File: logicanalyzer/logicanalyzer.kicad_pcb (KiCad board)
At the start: 2 copper layers, 82.5 x 83.8 mm, 76 parts, among them J1 Conn_02x17_Odd_Even, J2 Conn_01x30_Pin, U1 74HC04, U10 74151, U2 74HC595, U3 74HC595, U4 74HC86, U5 74151, U6 74LS32, U7 74HC86, U8 74151

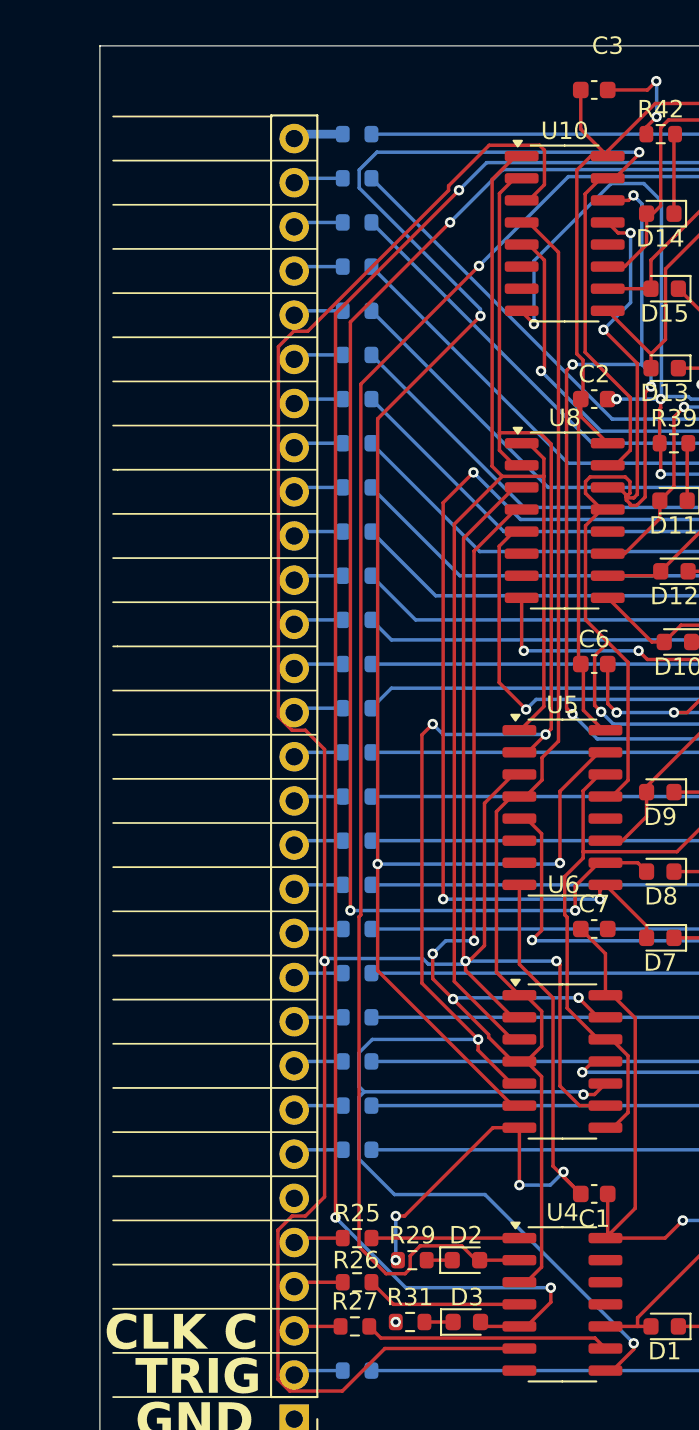
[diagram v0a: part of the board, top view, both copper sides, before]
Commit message: Schematic changes
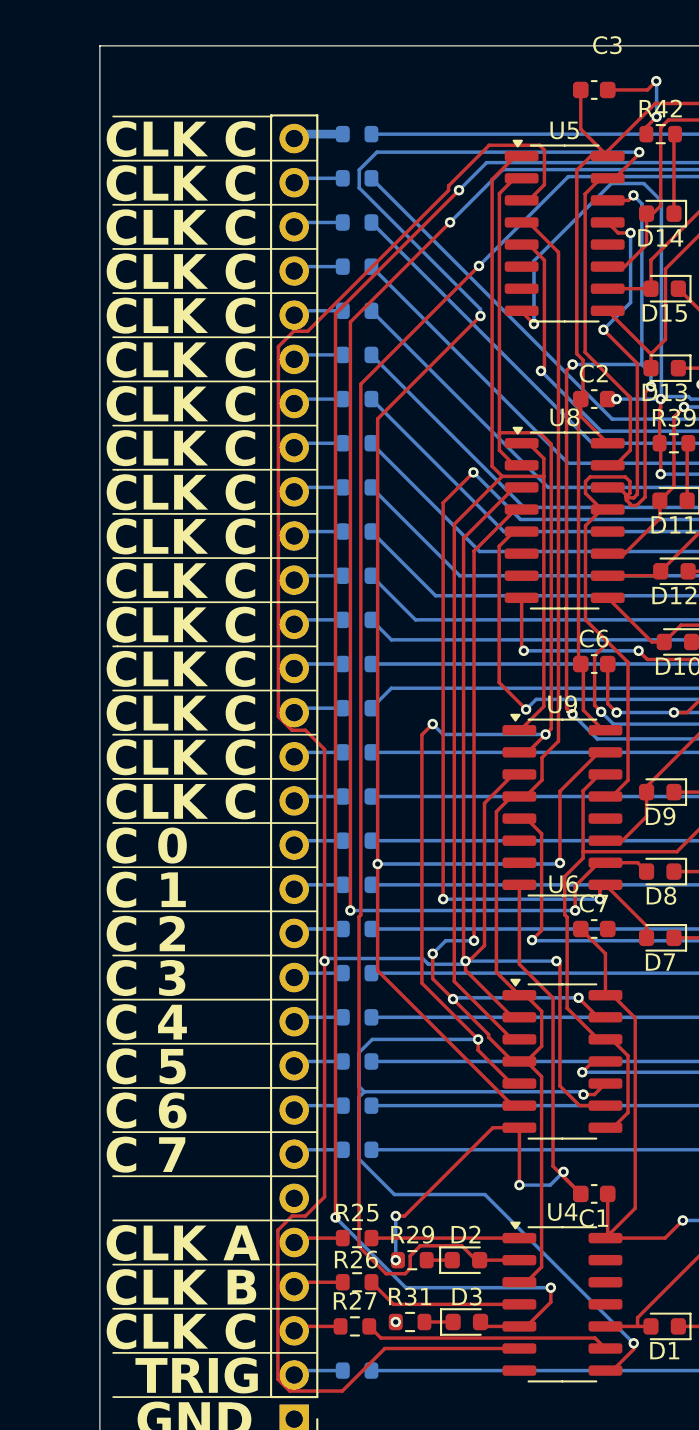
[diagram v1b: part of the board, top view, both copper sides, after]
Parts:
- removed U10: 74151, Package_SO:SOIC-16_3.9x9.9mm_P1.27mm
- added U9: 74HC251, Package_SO:SOIC-16_3.9x9.9mm_P1.27mm, F.Cu at (71.1, 92.1)
- R1, R10, R11, R12, R13, R14, R15, R16, R17, R18, R19, R2, R20, R21, R22, R23, R24, R25, R26, R27, R28, R29, R3, R30, R31, R32, R33, R34, R35, R36, R37, R38, R39, R4, R40, R41, R42, R43, R5, R6, R7, R8, R9: value 33k -> 500
- U5, U8: value 74151 -> 74HC251
- U6: value 74LS32 -> 74HC32
- moved U5 33.0 mm to (71.2, 59.1)
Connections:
- J1 pad 11: A7 -> A0
- J1 pad 12: A6 -> A1
- J1 pad 13: A5 -> A2
- J1 pad 14: A4 -> A3
- J1 pad 15: A3 -> A4
- J1 pad 16: A2 -> A5
- J1 pad 17: A1 -> A6
- J1 pad 18: A0 -> A7
- J1 pad 19: B7 -> B0
- J1 pad 20: B6 -> B1
- J1 pad 21: B5 -> B2
- J1 pad 22: B4 -> B3
- J1 pad 23: B3 -> B4
- J1 pad 24: B2 -> B5
- J1 pad 25: B1 -> B6
- J1 pad 26: B0 -> B7
- J1 pad 27: C7 -> C0
- J1 pad 28: C6 -> C1
- J1 pad 29: C5 -> C2
- J1 pad 30: C4 -> C3
- J1 pad 31: C3 -> C4
- J1 pad 32: C2 -> C5
- J1 pad 33: C1 -> C6
- J1 pad 34: C0 -> C7
- J2 pad 1: unconnected-(J2-Pin_1-Pad1) -> GND
- R1 pad 2: A6 -> A1
- R10 pad 2: B5 -> B2
- R11 pad 2: B4 -> B3
- R12 pad 2: B3 -> B4
- R13 pad 2: B2 -> B5
- R14 pad 2: B1 -> B6
- R15 pad 2: B0 -> B7
- R16 pad 2: C7 -> C0
- R17 pad 2: C6 -> C1
- R18 pad 2: C5 -> C2
- R19 pad 2: C4 -> C3
- R2 pad 2: A5 -> A2
- R20 pad 2: C3 -> C4
- R21 pad 2: C2 -> C5
- R22 pad 2: C1 -> C6
- R23 pad 2: C0 -> C7
- R3 pad 2: A4 -> A3
- R30 pad 2: A7 -> A0
- R4 pad 2: A3 -> A4
- R5 pad 2: A2 -> A5
- R6 pad 2: A1 -> A6
- R7 pad 2: A0 -> A7
- R8 pad 2: B7 -> B0
- R9 pad 2: B6 -> B1
- U5 pad 10: SMPL_A_is_C -> SMPL_C_is_C
- U5 pad 11: SMPL_A_is_B -> SMPL_C_is_B
- U5 pad 9: SMPL_A_is_A+C -> SMPL_C_is_A+C
- U7 pad 1: Net-(U5-Q) -> Net-(U9-Q)
- U7 pad 9: Net-(U10-Q) -> Net-(U5-Q)
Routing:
- net Net-(U9-Q): track 0.00 -> 65.7 mm, vias 0 -> 4
- net Net-(U10-Q): track 41.7 -> 0.00 mm, vias 2 -> 0
- net Net-(U5-Q): track 65.7 -> 41.7 mm, vias 4 -> 2
- net C7: track 53.8 -> 60.5 mm
- net C0: track 60.5 -> 53.8 mm
- net A6: track 60.4 -> 54.8 mm
- net A1: track 54.8 -> 60.4 mm
- net C5: track 54.8 -> 59.5 mm
- net C2: track 59.5 -> 54.8 mm
- net B4: track 55.2 -> 51.7 mm
- net B3: track 51.7 -> 55.2 mm
- net B6: track 56.2 -> 52.7 mm
- net B1: track 52.7 -> 56.2 mm
- net A4: track 59.4 -> 55.9 mm
- net A3: track 55.9 -> 59.4 mm
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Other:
- board text added: "C 0"
- board text added: "C 1"
- board text added: "C 2"
- board text added: "C 3"
- board text added: "C 4"
- board text added: "C 5"
- board text added: "C 6"
- board text added: "C 7"
- board text added: "CLK A"
- board text added: "CLK B"

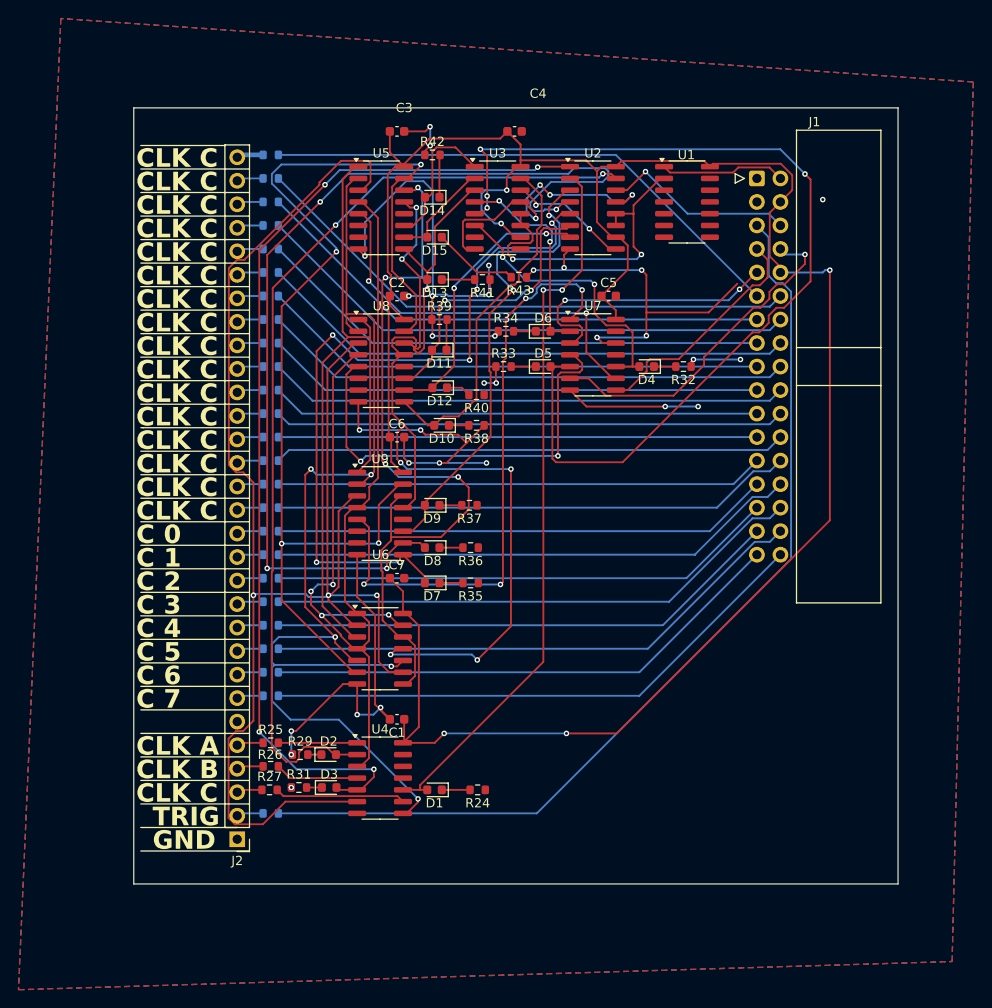
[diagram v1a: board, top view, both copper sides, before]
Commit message: Schematic changes
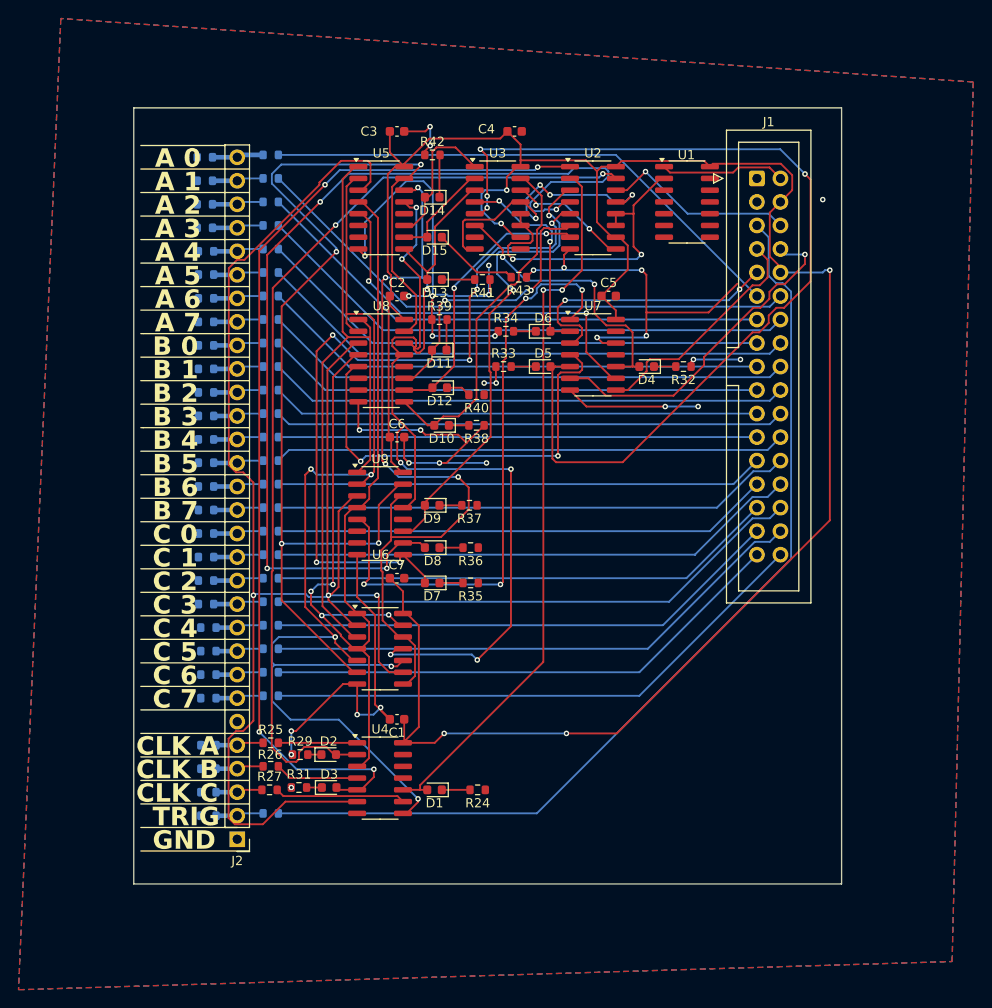
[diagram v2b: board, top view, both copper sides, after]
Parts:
- added R44: 100k, Resistor_SMD:R_0603_1608Metric, B.Cu at (52.5, 124.7)
- added R45: 100k, Resistor_SMD:R_0603_1608Metric, B.Cu at (52.5, 122.2)
- added R46: 100k, Resistor_SMD:R_0603_1608Metric, B.Cu at (52.5, 119.6)
- added R47: 100k, Resistor_SMD:R_0603_1608Metric, B.Cu at (52.5, 117.1)
- added R48: 100k, Resistor_SMD:R_0603_1608Metric, B.Cu at (52.5, 112.0)
- added R49: 100k, Resistor_SMD:R_0603_1608Metric, B.Cu at (52.5, 109.5)
- added R50: 100k, Resistor_SMD:R_0603_1608Metric, B.Cu at (52.5, 106.9)
- added R51: 100k, Resistor_SMD:R_0603_1608Metric, B.Cu at (52.5, 104.4)
- added R52: 100k, Resistor_SMD:R_0603_1608Metric, B.Cu at (52.3, 101.9)
- added R53: 100k, Resistor_SMD:R_0603_1608Metric, B.Cu at (52.3, 99.3)
- added R54: 100k, Resistor_SMD:R_0603_1608Metric, B.Cu at (52.3, 96.8)
- added R55: 100k, Resistor_SMD:R_0603_1608Metric, B.Cu at (52.3, 94.2)
- added R56: 100k, Resistor_SMD:R_0603_1608Metric, B.Cu at (52.3, 91.7)
- added R57: 100k, Resistor_SMD:R_0603_1608Metric, B.Cu at (52.3, 89.2)
- added R58: 100k, Resistor_SMD:R_0603_1608Metric, B.Cu at (52.3, 86.6)
- added R59: 100k, Resistor_SMD:R_0603_1608Metric, B.Cu at (52.3, 84.1)
- added R60: 100k, Resistor_SMD:R_0603_1608Metric, B.Cu at (52.3, 81.5)
- added R61: 100k, Resistor_SMD:R_0603_1608Metric, B.Cu at (52.3, 79.0)
- added R62: 100k, Resistor_SMD:R_0603_1608Metric, B.Cu at (52.3, 76.5)
- added R63: 100k, Resistor_SMD:R_0603_1608Metric, B.Cu at (52.3, 73.9)
- added R64: 100k, Resistor_SMD:R_0603_1608Metric, B.Cu at (52.3, 71.4)
- added R65: 100k, Resistor_SMD:R_0603_1608Metric, B.Cu at (52.3, 68.8)
- added R66: 100k, Resistor_SMD:R_0603_1608Metric, B.Cu at (52.3, 66.3)
- added R67: 100k, Resistor_SMD:R_0603_1608Metric, B.Cu at (52.3, 63.8)
- added R68: 100k, Resistor_SMD:R_0603_1608Metric, B.Cu at (52.1, 61.2)
- added R69: 100k, Resistor_SMD:R_0603_1608Metric, B.Cu at (52.1, 58.7)
- added R70: 100k, Resistor_SMD:R_0603_1608Metric, B.Cu at (52.1, 56.1)
- added R71: 100k, Resistor_SMD:R_0603_1608Metric, B.Cu at (52.1, 53.6)
- J1: footprint Connector_IDC:IDC-Header_2x17_P2.54mm_Horizontal -> Connector_IDC:IDC-Header_2x17_P2.54mm_Vertical
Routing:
- net Net-(J2-Pin_30): track 2.54 -> 5.21 mm
- net Net-(J2-Pin_29): track 2.54 -> 5.21 mm
- net Net-(J2-Pin_28): track 2.54 -> 5.21 mm
- net Net-(J2-Pin_27): track 2.54 -> 5.21 mm
- net Net-(J2-Pin_25): track 2.54 -> 5.09 mm
- net Net-(J2-Pin_17): track 2.54 -> 5.09 mm
- net Net-(J2-Pin_26): track 2.54 -> 5.08 mm
- net Net-(J2-Pin_24): track 2.54 -> 5.08 mm
- net Net-(J2-Pin_23): track 2.54 -> 5.08 mm
- net Net-(J2-Pin_22): track 2.54 -> 5.08 mm
- net Net-(J2-Pin_21): track 2.54 -> 5.08 mm
- net Net-(J2-Pin_20): track 2.54 -> 5.08 mm
- net Net-(J2-Pin_19): track 2.54 -> 5.08 mm
- net Net-(J2-Pin_18): track 2.54 -> 5.08 mm
- net Net-(J2-Pin_16): track 2.54 -> 5.08 mm
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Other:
- board size 82.5 x 83.8 mm -> 76.5 x 83.8 mm
- board text added: "A 0"
- board text added: "A 1"
- board text added: "A 2"
- board text added: "A 3"
- board text added: "A 4"
- board text added: "A 5"
- board text added: "A 6"
- board text added: "A 7"
- board text added: "B 0"
- board text added: "B 1"
- board text added: "B 2"
- board text added: "B 3"
- board text added: "B 4"
- board text added: "B 5"
- board text added: "B 6"
- board text added: "B 7"

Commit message: Add ROM dumps
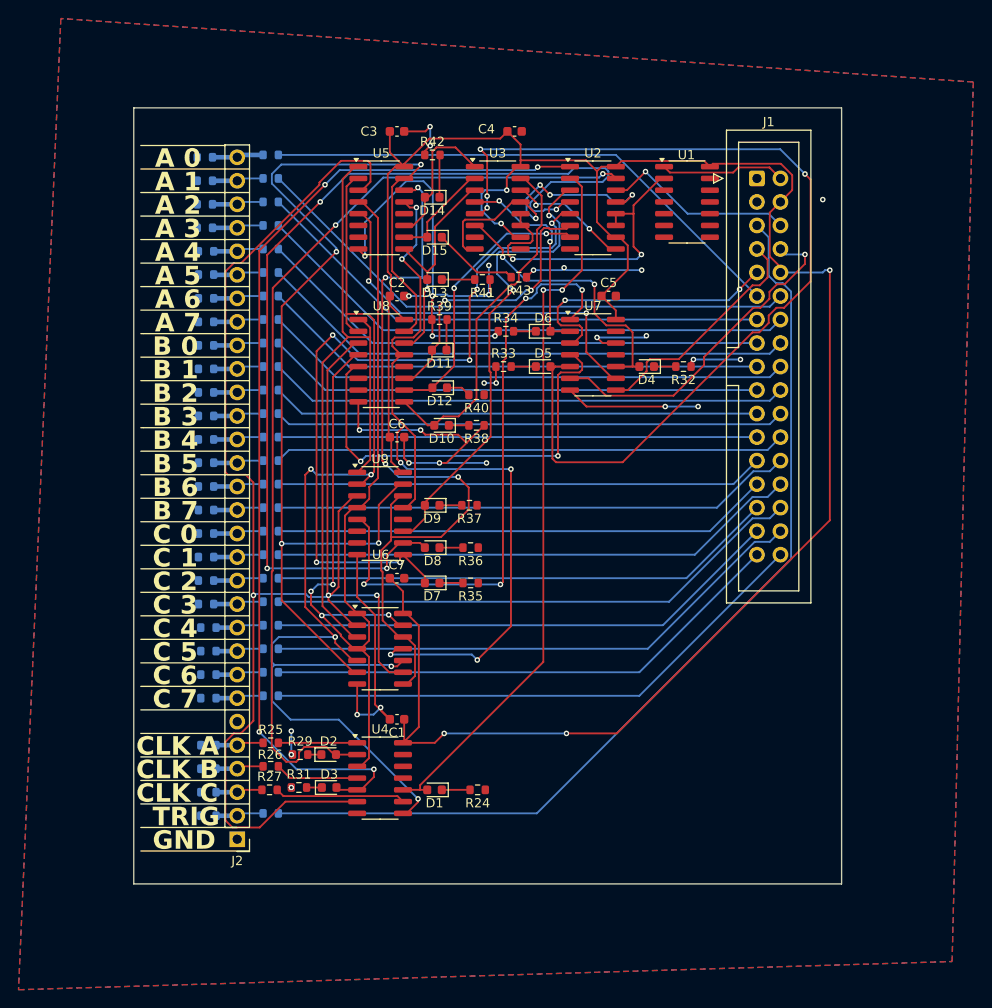
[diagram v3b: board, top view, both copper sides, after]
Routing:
- net GND: track 227.0 -> 197.1 mm
- net A+B+C: track 93.6 -> 90.8 mm
- net B+C: track 93.2 -> 91.1 mm
- net B: track 171.7 -> 173.5 mm
